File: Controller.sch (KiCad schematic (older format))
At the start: 21 parts

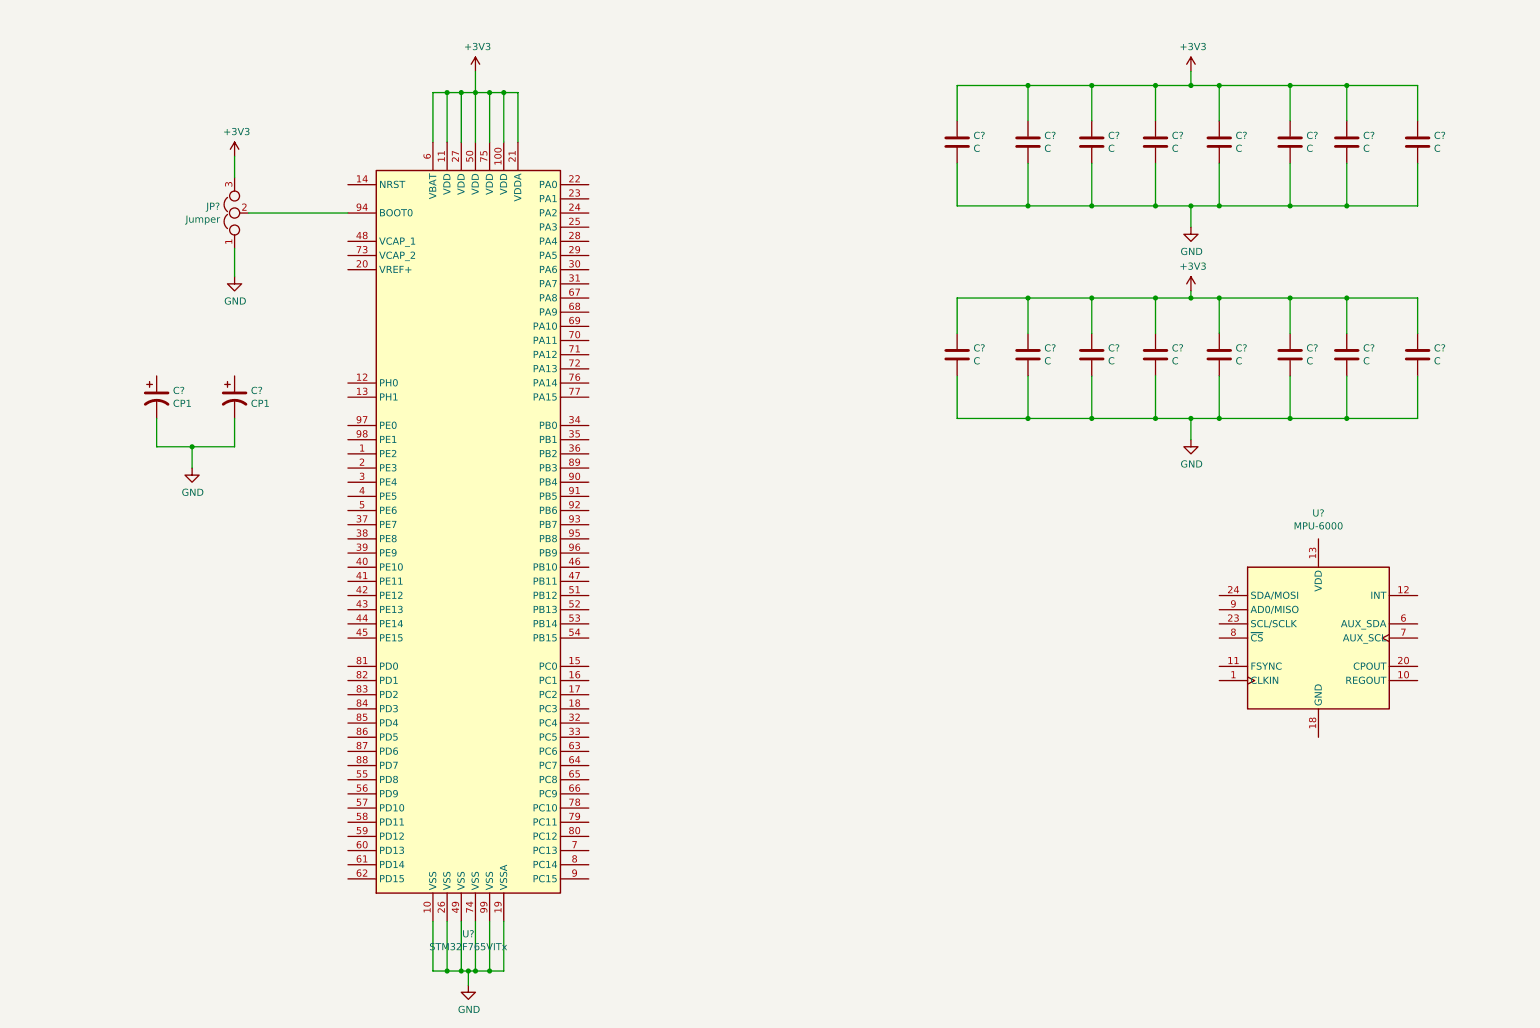
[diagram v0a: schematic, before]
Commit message: Added all ICs expcept Power supply
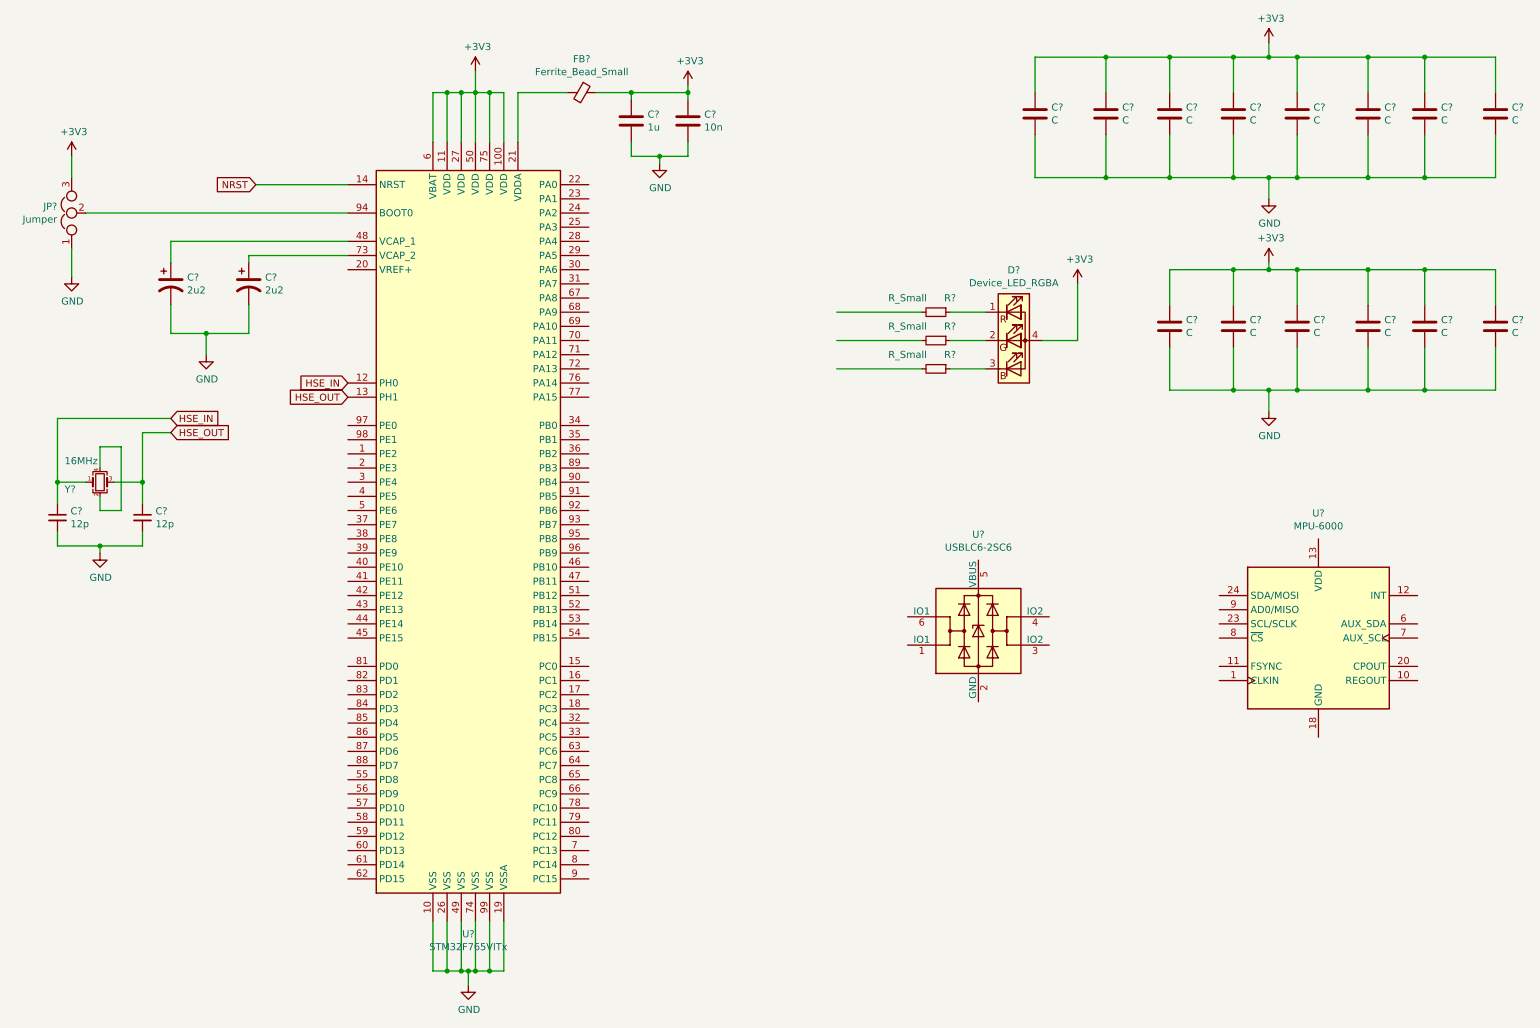
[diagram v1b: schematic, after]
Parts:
- removed C? (x2): C, symbol Device:C
- added C?: 1u, symbol Device:C
- added C?: 10n, symbol Device:C
- added C? (x2): 12p, symbol Device:C_Small
- added D?: Device_LED_RGBA, symbol RBoard-cache:Device_LED_RGBA
- added FB?: Ferrite_Bead_Small, symbol Device:Ferrite_Bead_Small
- added R? (x3): R_Small, symbol Device:R_Small
- added U?: USBLC6-2SC6, Package_TO_SOT_SMD:SOT-23-6, symbol Power_Protection:USBLC6-2SC6
- added Y?: 16MHz, symbol RBoard-cache:Device_Crystal_GND24_Small
- C? (x2): value CP1 -> 2u2
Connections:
- net +3V3: now also C?.1, C?.1, D?.4 (A), FB?.1; no longer U?.21 (VDDA)
- net GND: now also C?.2, C?.2, C?.2, C?.2
- net HSE_IN: now reaches U?.12 (PH0)
- net HSE_IN: now also C?.1, Y?.1
- net HSE_OUT: now reaches U?.13 (PH1)
- net HSE_OUT: now also C?.1, Y?.3
- net NRST: now reaches U?.14 (NRST)
- net at U?.48 (VCAP_1): now also C?.1
- net at U?.73 (VCAP_2): now also C?.1
- new net: FB?.2, U?.21 (VDDA)
- new net: Y?.2, Y?.4
- new net: D?.1 (RK), R?.1
- new net: D?.2 (GK), R?.1
- new net: D?.3 (BK), R?.1
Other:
- moved on the sheet: C?, JP?
